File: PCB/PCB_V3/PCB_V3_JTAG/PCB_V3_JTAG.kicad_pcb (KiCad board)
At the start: 2 copper layers, 74 parts, among them J1 ESP_Left, J11 ACS2_pins, J12 ACS4_Pins, J13 ACS2_Screw, J14 ACS4_Screw, J15 MCP_VCC_LINE, J16 AMS_IP_Pins, J17 AMS_OP_Pins, J18 BC1_IN+, J19 BC1_IN-, J2 ESP_Right, J20 BC3_IN+, J21 BC3_IN-, J22 BC1_OUT+, J23 BC1_OUT-, J24 BC3_OUT+, J25 BC3_OUT-, J26 BC2_IN+, J27 BC2_IN-, J28 BC5_IN+, J29 BC5_IN-, J3 ACS1_Pins, J30 BC2_OUT+, J31 BC2_OUT-, J32 BC5_OUT+, J33 BC5_OUT-, J34 LED_LHS_JTAG, J35 LED_RHS_JTAG, J4 ACS3_Pins, J44 STATIC_LED_1, J45 STATIC_LED_2, J46 I/P_Terminal, J47 Battery_Terminal, J5 ACS3_Screw, J6 ACS1_Screw, J7 Conn_02x07_Counter_Clockwise, J8 MCP_A0_B0, Q1 IRLZ44N, Q10 IRLZ44N, Q2 IRLZ44N, Q3 IRLZ44N, Q4 IRLZ44N, Q5 IRLZ44N, Q6 IRLZ44N, Q7 IRLZ44N, Q8 IRLZ44N, Q9 IRLZ44N

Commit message: misc.
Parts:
- added J10: LHS_Arrow_+ve, Connector_PinSocket_2.54mm:PinSocket_1x05_P2.54mm_Vertical, F.Cu at (140.5, 41.3)
- added J36: RHS_Arrow_+ve, Connector_PinSocket_2.54mm:PinSocket_1x05_P2.54mm_Vertical, F.Cu at (154.2, 41.3)
- added J37: LAN8720_pins_1, Connector_PinSocket_2.54mm:PinSocket_1x07_P2.54mm_Vertical, F.Cu at (221.9, 101.5)
- added J9: MCP_A0, Connector_PinSocket_2.54mm:PinSocket_1x10_P2.54mm_Vertical, F.Cu at (135.9, 41.3)
- J34: value LED_LHS_JTAG -> LHS_Arrow_-ve; footprint Connector_PinSocket_2.54mm:PinSocket_2x05_P2.54mm_Vertical -> Connector_PinSocket_2.54mm:PinSocket_1x05_P2.54mm_Vertical
- J35: value LED_RHS_JTAG -> RHS_Arrow_-ve; footprint Connector_PinSocket_2.54mm:PinSocket_2x05_P2.54mm_Vertical -> Connector_PinSocket_2.54mm:PinSocket_1x05_P2.54mm_Vertical
- J7: value Conn_02x07_Counter_Clockwise -> LAN8720_pins_2; footprint Connector_PinSocket_2.54mm:PinSocket_2x07_P2.54mm_Vertical -> Connector_PinSocket_2.54mm:PinSocket_1x07_P2.54mm_Vertical
- J8: value MCP_A0_B0 -> MCP_B0; footprint Connector_PinSocket_2.54mm:PinSocket_2x10_P2.54mm_Vertical -> Connector_PinSocket_2.54mm:PinSocket_1x10_P2.54mm_Vertical
- moved J2 147.2 mm to (210.0, 105.0)
- moved J1 127.4 mm to (184.6, 105.0)
- moved J7 125.7 mm to (221.9, 106.1), turned to 90 degrees
- moved J34 65.8 mm to (145.1, 41.3)
- moved J35 64.6 mm to (149.7, 41.3)
- moved J8 24.2 mm to (131.3, 41.3)
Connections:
- J34 pad 1: /LHS_LED_IP+ -> /LHS_LED_1
- J34 pad 2: /LHS_LED_1 -> /LHS_LED_2
- J34 pad 3: /LHS_LED_IP+ -> /LHS_LED_3
- J34 pad 4: /LHS_LED_2 -> /LHS_LED_4
- J34 pad 5: /LHS_LED_IP+ -> /LHS_LED_5
- J35 pad 1: /RHS_LED_IP+ -> /RHS_LED_1
- J35 pad 2: /RHS_LED_1 -> /RHS_LED_2
- J35 pad 3: /RHS_LED_IP+ -> /RHS_LED_3
- J35 pad 4: /RHS_LED_2 -> /RHS_LED_4
- J35 pad 5: /RHS_LED_IP+ -> /RHS_LED_5
- J8 pad 3: /A0 -> /B0
- J8 pad 4: /A1 -> /B1
- J8 pad 5: /A2 -> /B2
- J8 pad 6: /A3 -> /B3
- J8 pad 7: /A4 -> /B4

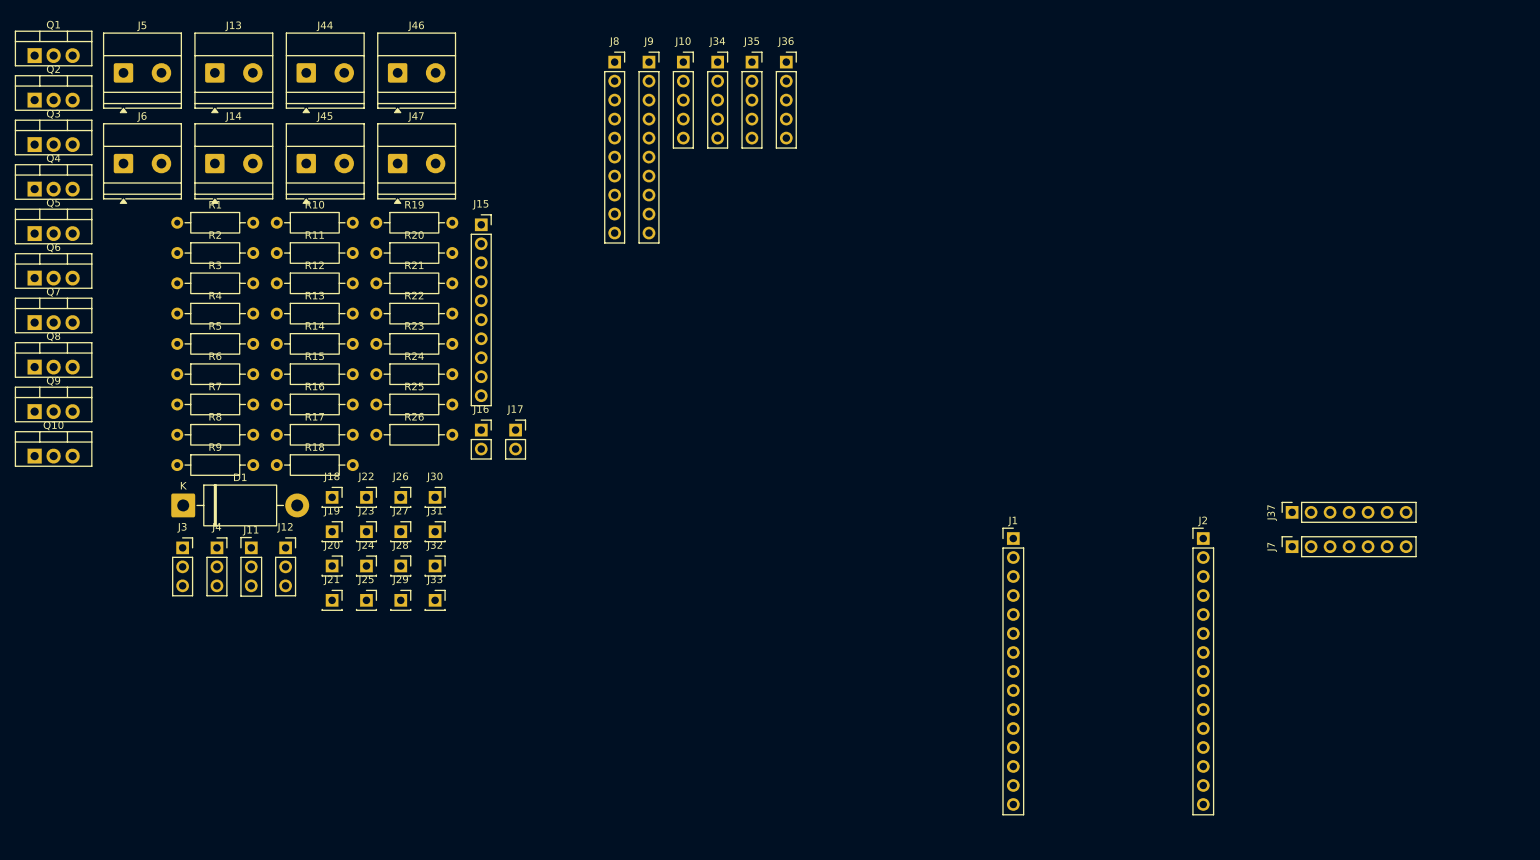
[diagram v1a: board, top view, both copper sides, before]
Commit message: PCB commit
1. Pins need to be named
2. There are courtyard errors that need to be looked into for the split connectors (2x0)
3. Connections of the negative of the LEDs to the MOSFETs need to be made
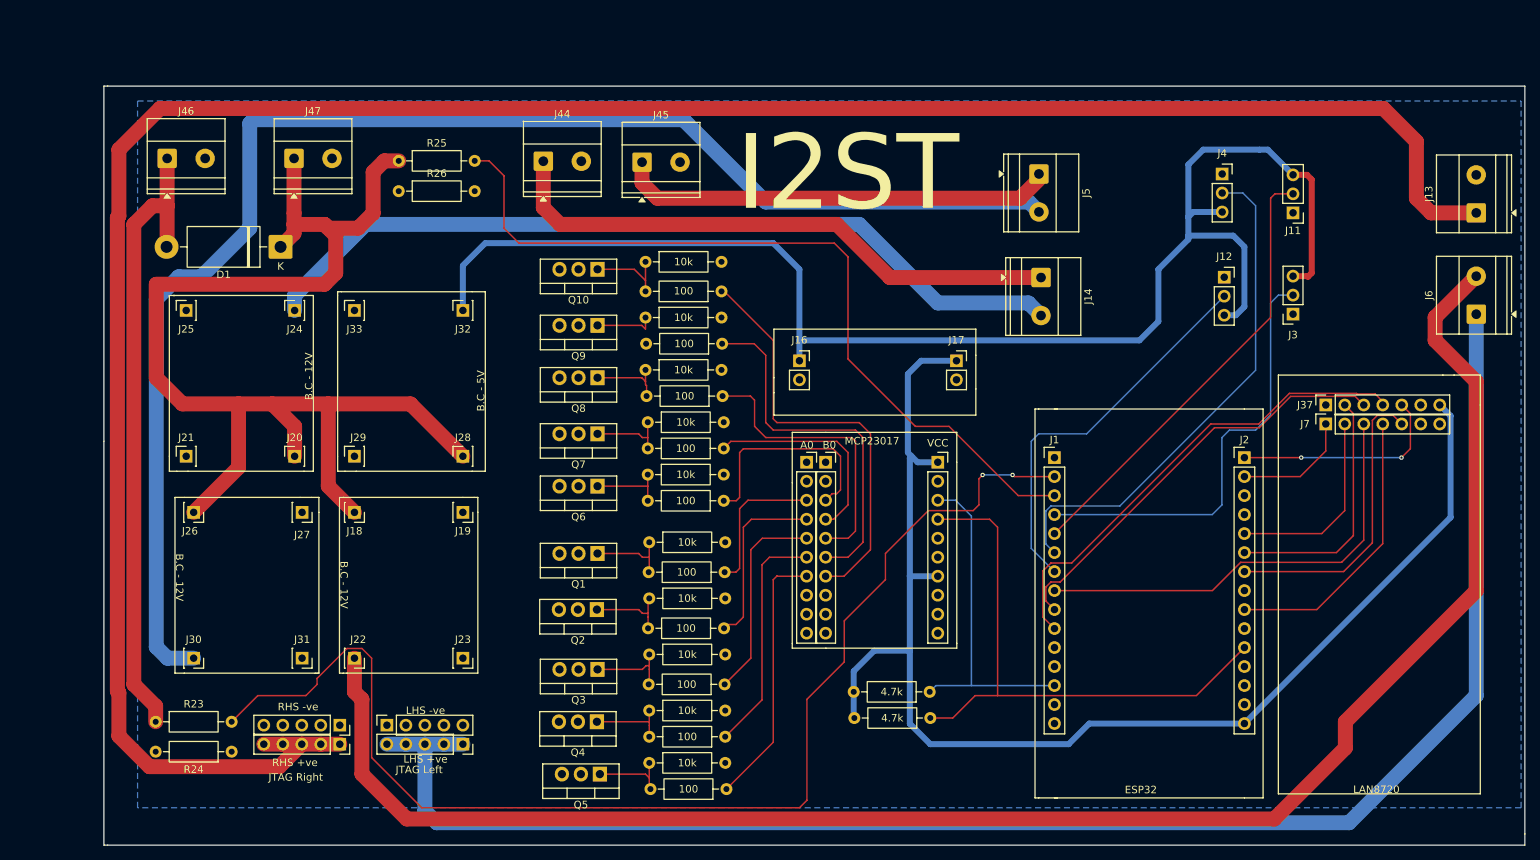
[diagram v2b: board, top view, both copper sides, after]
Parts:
- moved J6 182.0 mm to (246.5, 75.0), turned to 90 degrees
- moved J13 169.7 mm to (246.5, 61.5), turned to 90 degrees
- moved J3 151.7 mm to (222.0, 75.0), turned to 180 degrees
- moved J11 146.3 mm to (222.0, 61.5), turned to 180 degrees
- moved J4 143.4 mm to (212.5, 56.3)
- moved J12 130.6 mm to (212.8, 70.1)
- moved J5 123.2 mm to (188.0, 56.3), turned to -90 degrees
- moved J14 111.5 mm to (188.3, 70.1), turned to -90 degrees
- moved J36 109.0 mm to (94.5, 132.5), turned to -90 degrees
- moved Q5 104.6 mm to (129.3, 136.5), turned to 180 degrees
- moved J35 104.4 mm to (94.5, 130.0), turned to -90 degrees
- moved Q4 103.6 mm to (128.9, 129.5), turned to 180 degrees
- moved Q3 102.9 mm to (129.0, 122.5), turned to 180 degrees
- moved Q2 101.5 mm to (128.9, 114.5), turned to 180 degrees
- moved Q1 100.5 mm to (129.0, 107.0), turned to 180 degrees
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- renumbered R4 to 100, R16 to 100, R19 to 100, R18 to 100, R1 to 100, R17 to 100, R5 to 100, R3 to 100, R2 to 100, R20 to 100, R8 to 10k, R6 to 10k, R11 to 10k, R14 to 10k, R10 to 10k, R7 to 10k, R12 to 10k, R15 to 10k, R13 to 10k, R9 to 10k, R21 to 4.7k, R22 to 4.7k
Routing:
- net /RHS_LED_IP+: track 0.00 -> 310.1 mm
- net /12V_LR: track 0.00 -> 228.7 mm
- net /LHS_LED_IP+: track 0.00 -> 218.4 mm
- net /5V: track 0.00 -> 195.9 mm
- net /12V_STATIC1: track 0.00 -> 193.4 mm
- net /AMS_OP+: track 0.00 -> 179.2 mm
- net /PSU_VD: track 0.00 -> 164.9 mm, vias 0 -> 2
- net /MAIN_OP: track 0.00 -> 164.5 mm
- net /12V_STATIC2: track 0.00 -> 110.8 mm
- net /BATT_VD: track 0.00 -> 108.2 mm
- net /14.5: track 0.00 -> 85.1 mm
- net /D4: track 0.00 -> 76.8 mm
- net /STATIC2+: track 0.00 -> 76.6 mm
- net /D32: track 0.00 -> 69.1 mm
- net /D27: track 0.00 -> 64.5 mm
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- added copper zone on B.Cu, net GND
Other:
- board outline added: 190 x 101.5 mm
- board text added: "A0"
- board text added: "B.C - 12V"
- board text added: "B.C - 5V"
- board text added: "B0"
- board text added: "ESP32"
- board text added: "I2ST"
- board text added: "JTAG Left"
- board text added: "JTAG Right"
- board text added: "LAN8720"
- board text added: "LHS +ve"
- board text added: "LHS -ve"
- board text added: "MCP23017"
- board text added: "RHS +ve"
- board text added: "RHS -ve"
- board text added: "VCC"

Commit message: Uploading the final iteration of the PCB design files
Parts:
- added TP1: 12V_Arrows, TestPoint:TestPoint_Pad_D1.5mm, F.Cu at (155.0, 52.2)
- added TP2: 12V_Static_2, TestPoint:TestPoint_Pad_D1.5mm, F.Cu at (160.0, 52.2)
- added TP3: 12V_Static_1, TestPoint:TestPoint_Pad_D1.5mm, F.Cu at (165.5, 52.2)
- added TP4: 5V, TestPoint:TestPoint_Pad_D1.5mm, F.Cu at (170.0, 52.2)
- renumbered 100 to R1, 10k to R10, 10k to R11, 10k to R12, 10k to R13, 10k to R14, 10k to R15, 100 to R16, 100 to R17, 100 to R18, 100 to R19, 100 to R2, 100 to R20, 4.7k to R21, 4.7k to R22, 100 to R3, 100 to R4, 100 to R5, 10k to R6, 10k to R7, 10k to R8, 10k to R9
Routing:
- net /12V_LR: track 228.7 -> 357.2 mm, vias 0 -> 4
- net /RHS_LED_5: track 0.65 -> 98.9 mm
- net /RHS_LED_4: track 0.00 -> 79.7 mm
- net /RHS_LED_3: track 0.00 -> 73.9 mm
- net /12V_STATIC2: track 110.8 -> 177.5 mm, vias 0 -> 1
- net /RHS_LED_2: track 0.00 -> 62.3 mm
- net /RHS_LED_1: track 0.00 -> 50.1 mm
- net /LHS_LED_1: track 0.00 -> 41.8 mm
- net /5V: track 195.9 -> 235.5 mm, vias 0 -> 3
- net /LHS_LED_2: track 0.00 -> 34.7 mm
- net /LHS_LED_3: track 0.00 -> 25.3 mm
- net /LHS_LED_5: track 0.00 -> 25.2 mm
- net /LHS_LED_4: track 0.17 -> 25.1 mm
- net /AMS_OP+: track 179.2 -> 189.5 mm
- net /12V_STATIC1: track 193.4 -> 202.0 mm, vias 0 -> 3
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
